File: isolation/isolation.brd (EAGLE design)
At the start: 74.5 x 72.7 mm, 91 parts, among them IC1 XTLV61048DBVR, IC2 SN74HC14PWR, IC3 SN74HCS32BQAR, IC4 SN74HCS08DYYR, IC5 FDN359BN, IC6 FDN359BN, IC7 FDN359BN, IC8 FDN359BN, J1 S4B-PH-K-S(LF)(SN), J2 S4B-PH-K-S(LF)(SN), J3 S2B-PH-K-S(LF)(SN), J4 S2B-PH-K-S(LF)(SN), J5 S2B-PH-K-S(LF)(SN), J7 217175-0001

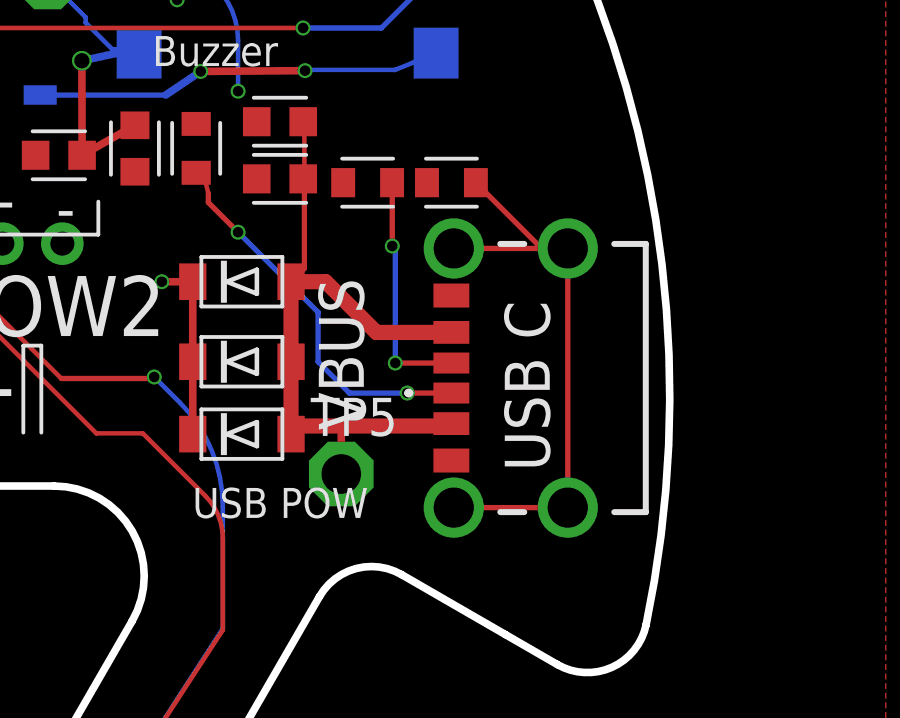
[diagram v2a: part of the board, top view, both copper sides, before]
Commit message: swap usb c (again)
now using USB4105-GF-A-120, consistent with WALLY
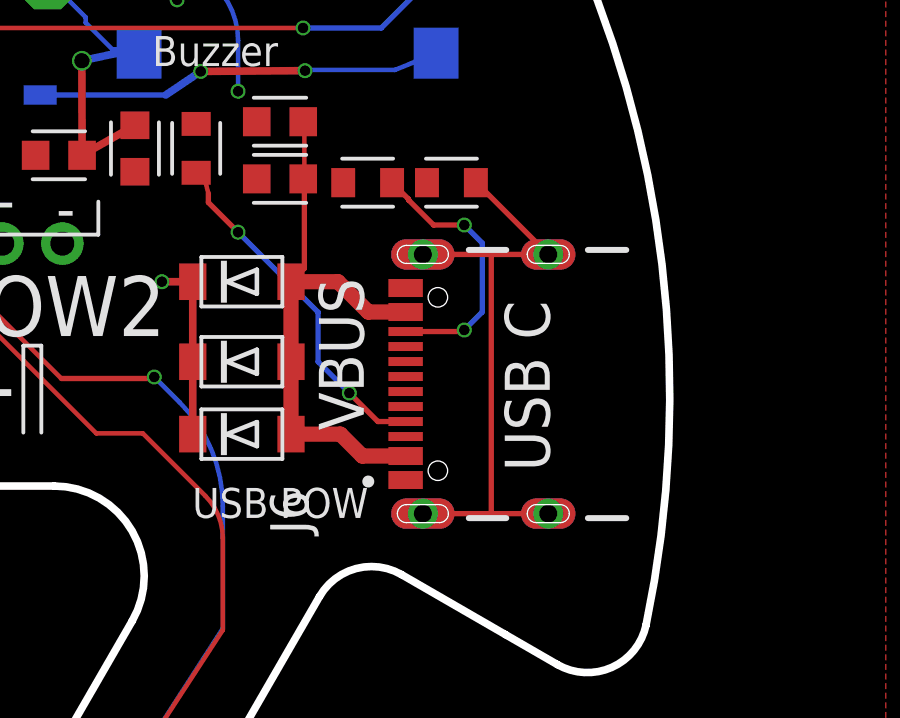
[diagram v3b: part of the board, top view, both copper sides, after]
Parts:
- removed J7: 217175-0001, SamacSys_Parts:2171750001
- removed TP5: PTR1PAD1-13, testpad:P1-13
- added J6: USB4105-GF-A, USB4105-GF-A:GCT_USB4105-GF-A
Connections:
- net CC1: now also J6.A5; no longer J7.A5
- net CC2: now also J6.B5; no longer J7.B5
- net GND: now also J6.A1_B12, J6.B1_A12; no longer J7.A12, J7.B12
- net SHLD: now also J6.SH1, J6.SH2, J6.SH3, J6.SH4; no longer J7.MH1, J7.MH2, J7.MH3, J7.MH4
- net VBUS: now also J6.A4_B9, J6.B4_A9; no longer J7.A9, J7.B9, TP5.TP
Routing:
- net VBUS: track 23.8 -> 19.0 mm
- net CC1: track 12.8 -> 11.7 mm
- net CC2: track 7.93 -> 8.99 mm
- net SHLD: track 19.3 -> 20.4 mm
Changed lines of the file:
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@@
 <attribute name="VOLTAGE_RATING" value="" x="11.318" y="21.685" size="1.778" layer="27" rot="R90" display="off"/>
 </element>
-<element name="J7" library="SamacSys_Parts" package="2171750001" value="217175-0001" x="33" y="0.6" smashed="yes" rot="R90">
-<attribute name="ARROW_PART_NUMBER" value="" x="33" y="0.6" size="1.778" layer="27" rot="R90" display="off"/>
-<attribute name="ARROW_PRICE-STOCK" value="" x="33" y="0.6" size="1.778" layer="27" rot="R90" display="off"/>
-<attribute name="DESCRIPTION" value="Connector USB Type C Female 6Positions 0.5mm Right Angle SMT Embossed T/R - Tape and Reel" x="33" y="0.6" size="1.778" layer="27" rot="R90" display="off"/>
-<attribute name="HEIGHT" value="3.46mm" x="33" y="0.6" size="1.778" layer="27" rot="R90" display="off"/>
-<attribute name="MANUFACTURER_NAME" value="Molex" x="33" y="0.6" size="1.778" layer="27" rot="R90" display="off"/>
-<attribute name="MANUFACTURER_PART_NUMBER" value="217175-0001" x="33" y="0.6" size="1.778" layer="27" rot="R90" display="off"/>
-<attribute name="MOUSER_PART_NUMBER" value="538-217175-0001" x="33" y="0.6" size="1.778" layer="27" rot="R90" display="off"/>
-<attribute name="MOUSER_PRICE-STOCK" value="https://www.mouser.co.uk/ProductDetail/Molex/217175-0001?qs=DRkmTr78QARWJMiqNnldSg%3D%3D" x="33" y="0.6" size="1.778" layer="27" rot="R90" display="off"/>
-<attribute name="VALUE" x="32.748" y="0.6" size="1.27" layer="27" rot="R90" align="center"/>
-</element>
-<element name="TP5" library="testpad" library_urn="urn:adsk.eagle:library:385" package="P1-13" package3d_urn="urn:adsk.eagle:package:27946/1" override_package3d_urn="urn:adsk.eagle:package:44099355/2" override_package_urn="urn:adsk.eagle:footprint:27902/1" value="PTR1PAD1-13" x="26.3" y="-2.6" smashed="yes">
-<attribute name="NAME" x="25.284" y="-1.33" size="1.27" layer="25" ratio="10"/>
-<attribute name="POPULARITY" value="2" x="26.3" y="-2.6" size="1.778" layer="27" display="off"/>
-<attribute name="TP_SIGNAL_NAME" value="" x="26.3" y="-2.6" size="1.778" layer="27" display="off"/>
-<attribute name="VALUE" x="26.3" y="-2.6" size="0.0254" layer="27"/>
+<element name="J6" library="USB4105-GF-A" package="GCT_USB4105-GF-A" value="USB4105-GF-A" x="33.2" y="0.4" smashed="yes" rot="R90">
+<attribute name="CHECK_PRICES" value="https://www.snapeda.com/parts/USB4105GFA/Global+Connector+Technology/view-part/?ref=eda" x="33.2" y="0.4" size="1.778" layer="27" rot="R90" display="off"/>
+<attribute name="DESCRIPTION" value=" USB-C (USB TYPE-C) USB 2.0 Receptacle Connector 24 (16+8 Dummy) Position Surface Mount, Right Angle; Through Hole " x="33.2" y="0.4" size="1.778" layer="27" rot="R90" display="off"/>
+<attribute name="DIGIKEY_PART_NUMBER" value="2073-USB4105-GF-ATR-ND" x="33.2" y="0.4" size="1.778" layer="27" rot="R90" display="off"/>
+<attribute name="MF" value="Global Connector Technology" x="33.2" y="0.4" size="1.778" layer="27" rot="R90" display="off"/>
+<attribute name="MP" value="USB4105GFA" x="33.2" y="0.4" size="1.778" layer="27" rot="R90" display="off"/>
+<attribute name="NAME" x="25.2" y="-4.6" size="1.27" layer="25" rot="R90"/>
+<attribute name="PACKAGE" value="None" x="33.2" y="0.4" size="1.778" layer="27" rot="R90" display="off"/>
+<attribute name="SNAPEDA_LINK" value="https://www.snapeda.com/parts/USB4105GFA/Global+Connector+Technology/view-part/?ref=snap" x="33.2" y="0.4" size="1.778" layer="27" rot="R90" display="off"/>
+<attribute name="VALUE" x="26.7" y="-4.6" size="1.27" layer="27" rot="R90"/>
 </element>
 </elements>
@@
 <contactref element="C22" pad="1"/>
 <wire x1="-7.493" y1="18.3006" x2="-8.89" y2="16.51" width="0.1778" layer="1"/>
-<contactref element="J7" pad="A12"/>
-<contactref element="J7" pad="B12"/>
+<contactref element="J6" pad="A1_B12"/>
+<contactref element="J6" pad="B1_A12"/>
 </signal>
 <signal name="VBAT">
@@
 <signal name="SHLD">
 <contactref element="R13" pad="1"/>
-<contactref element="J7" pad="MH4"/>
-<contactref element="J7" pad="MH1"/>
-<contactref element="J7" pad="MH2"/>
-<contactref element="J7" pad="MH3"/>
-<wire x1="30.05" y1="-3.72" x2="33.85" y2="-3.72" width="0.1778" layer="1"/>
-<wire x1="33.85" y1="-3.72" x2="33.85" y2="4.92" width="0.1778" layer="1"/>
-<wire x1="33.85" y1="4.92" x2="33" y2="4.92" width="0.1778" layer="1"/>
-<wire x1="32.9792" y1="4.92" x2="30.05" y2="4.92" width="0.1778" layer="1"/>
-<wire x1="30.7872" y1="7.112" x2="32.9792" y2="4.92" width="0.1778" layer="1"/>
-<wire x1="32.9792" y1="4.92" x2="33" y2="4.92" width="0.1778" layer="1"/>
+<contactref element="J6" pad="SH2"/>
+<contactref element="J6" pad="SH3"/>
+<contactref element="J6" pad="SH4"/>
+<contactref element="J6" pad="SH1"/>
+<wire x1="29.02" y1="-3.92" x2="31.3" y2="-3.92" width="0.1778" layer="1"/>
+<wire x1="31.3" y1="-3.92" x2="33.2" y2="-3.92" width="0.1778" layer="1"/>
+<wire x1="29.02" y1="4.72" x2="31.3" y2="4.72" width="0.1778" layer="1"/>
+<wire x1="31.3" y1="4.72" x2="33.2" y2="4.72" width="0.1778" layer="1"/>
+<wire x1="33.2" y1="4.72" x2="30.808" y2="7.112" width="0.1778" layer="1"/>
+<wire x1="30.808" y1="7.112" x2="30.7872" y2="7.112" width="0.1778" layer="1"/>
+<wire x1="31.3" y1="4.72" x2="31.3" y2="-3.92" width="0.1778" layer="1"/>
 </signal>
 <signal name="CC2">
 <contactref element="R12" pad="1"/>
-<contactref element="J7" pad="B5"/>
 <wire x1="27.9932" y1="7.112" x2="28" y2="7.1052" width="0.1778" layer="1"/>
-<wire x1="28" y1="7.1052" x2="28" y2="5" width="0.1778" layer="1"/>
-<via x="28" y="5" extent="1-16" drill="0.35"/>
-<wire x1="28" y1="5" x2="28.1" y2="4.9" width="0.1778" layer="16"/>
-<wire x1="28.1" y1="4.9" x2="28.1" y2="1.1" width="0.1778" layer="16"/>
-<via x="28.1" y="1.1" extent="1-16" drill="0.35"/>
-<wire x1="28.1" y1="1.1" x2="29.97" y2="1.1" width="0.1778" layer="1"/>
+<contactref element="J6" pad="B5"/>
+<via x="30.4" y="5.7" extent="1-16" drill="0.35"/>
+<wire x1="27.9932" y1="7.112" x2="28.54155" y2="6.56365" width="0.1778" layer="1"/>
+<wire x1="28.54155" y1="6.56365" x2="28.54155" y2="6.53561875" width="0.1778" layer="1"/>
+<wire x1="28.54155" y1="6.53561875" x2="29.37716875" y2="5.7" width="0.1778" layer="1"/>
+<wire x1="29.37716875" y1="5.7" x2="30.4" y2="5.7" width="0.1778" layer="1"/>
+<wire x1="30.4" y1="5.7" x2="31" y2="5.1" width="0.1778" layer="16"/>
+<wire x1="31" y1="2.8" x2="30.4" y2="2.2" width="0.1778" layer="16"/>
+<via x="30.4" y="2.2" extent="1-16" drill="0.35"/>
+<wire x1="30.4" y1="2.2" x2="30.35" y2="2.15" width="0.1778" layer="1"/>
+<wire x1="30.35" y1="2.15" x2="28.445" y2="2.15" width="0.1778" layer="1"/>
+<wire x1="31" y1="5.1" x2="31" y2="2.8" width="0.1778" layer="16"/>
 </signal>
 <signal name="CC1">
@@
 <wire x1="25.527" y1="2.794" x2="25.527" y2="1.143" width="0.1778" layer="16"/>
 <wire x1="25.527" y1="2.794" x2="22.86" y2="5.461" width="0.1778" layer="16"/>
-<contactref element="J7" pad="A5"/>
 <wire x1="25.527" y1="1.143" x2="26.57" y2="0.1" width="0.1778" layer="16"/>
-<wire x1="26.57" y1="0.1" x2="28.5" y2="0.1" width="0.1778" layer="16"/>
-<via x="28.5" y="0.1" extent="1-16" drill="0.35"/>
-<wire x1="28.5" y1="0.1" x2="29.97" y2="0.1" width="0.1778" layer="1"/>
+<contactref element="J6" pad="A5"/>
+<via x="26.57" y="0.1" extent="1-16" drill="0.35"/>
+<wire x1="26.57" y1="0.1" x2="27.52" y2="-0.85" width="0.1778" layer="1"/>
+<wire x1="27.52" y1="-0.85" x2="28.445" y2="-0.85" width="0.1778" layer="1"/>
 </signal>
 <signal name="VBUS">
@@
 <wire x1="25.0698" y1="4.2553" x2="25.0698" y2="7.112" width="0.1778" layer="1"/>
 <wire x1="25.0698" y1="4.2553" x2="24.6245" y2="3.81" width="0.1778" layer="1"/>
-<wire x1="24.6245" y1="3.81" x2="25.781" y2="3.81" width="0.508" layer="1"/>
 <wire x1="24.6245" y1="1.143" x2="24.6245" y2="3.81" width="0.508" layer="1"/>
-<contactref element="J7" pad="A9"/>
-<contactref element="J7" pad="B9"/>
-<wire x1="27.471" y1="2.12" x2="29.97" y2="2.12" width="0.508" layer="1"/>
-<wire x1="25.781" y1="3.81" x2="27.471" y2="2.12" width="0.508" layer="1"/>
-<wire x1="29.97" y1="-0.92" x2="29.89" y2="-1" width="0.508" layer="1"/>
-<contactref element="TP5" pad="TP"/>
 <wire x1="24.6245" y1="1.143" x2="24.6245" y2="-1.27" width="0.508" layer="1"/>
-<wire x1="24.8945" y1="-1" x2="24.6245" y2="-1.27" width="0.508" layer="1"/>
-<wire x1="29.89" y1="-1" x2="26.3" y2="-1" width="0.508" layer="1"/>
-<wire x1="26.3" y1="-1" x2="24.8945" y2="-1" width="0.508" layer="1"/>
-<wire x1="26.3" y1="-2.6" x2="26.3" y2="-1" width="0.254" layer="1"/>
+<contactref element="J6" pad="A4_B9"/>
+<contactref element="J6" pad="B4_A9"/>
+<wire x1="27" y1="-2" x2="28.445" y2="-2" width="0.508" layer="1"/>
+<wire x1="24.6245" y1="-1.27" x2="26.27" y2="-1.27" width="0.508" layer="1"/>
+<wire x1="26.27" y1="-1.27" x2="27" y2="-2" width="0.508" layer="1"/>
+<wire x1="28.445" y1="2.8" x2="27.2" y2="2.8" width="0.508" layer="1"/>
+<wire x1="26.19" y1="3.81" x2="24.6245" y2="3.81" width="0.508" layer="1"/>
+<wire x1="27.2" y1="2.8" x2="26.19" y2="3.81" width="0.508" layer="1"/>
 </signal>
 <signal name="N$27">
@@
 <mfgpreviewcolor name="substratecolor" color="0xFF786E46"/>
 </mfgpreviewcolors>
+<errors>
+</errors>
 </board>
 </drawing>

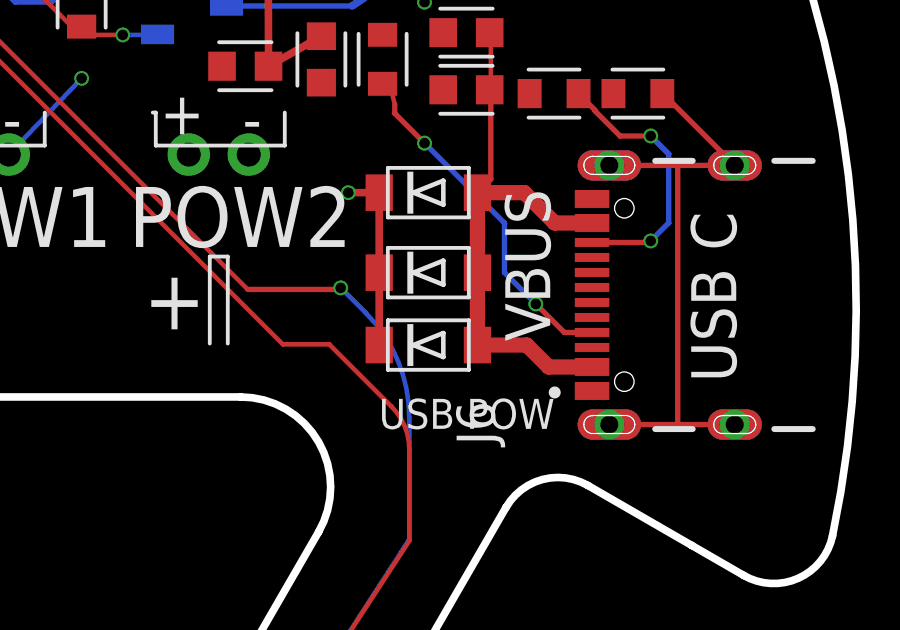
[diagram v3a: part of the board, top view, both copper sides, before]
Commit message: remove parallel vbus diodes
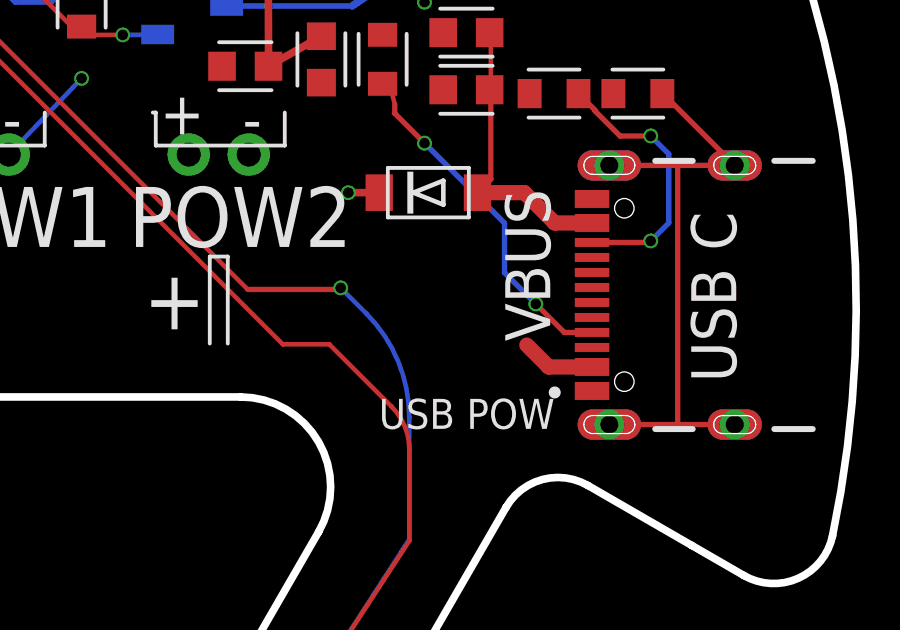
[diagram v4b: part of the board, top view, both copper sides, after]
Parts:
- removed D3, D4: USBDiode, adafruit:SOD-123FL
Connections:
- net VBAT: no longer D3.C, D4.C
- net VBUS: no longer D3.A, D4.A
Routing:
- net VBUS: track 19.0 -> 12.3 mm
- net VBAT: track 60.9 -> 55.8 mm
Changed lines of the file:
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@@
 <layer number="44" name="Drills" color="7" fill="1" visible="no" active="yes"/>
 <layer number="45" name="Holes" color="7" fill="1" visible="yes" active="yes"/>
-<layer number="46" name="Milling" color="3" fill="1" visible="no" active="yes"/>
+<layer number="46" name="Milling" color="3" fill="1" visible="yes" active="yes"/>
 <layer number="47" name="Measures" color="7" fill="1" visible="no" active="yes"/>
 <layer number="48" name="Document" color="7" fill="1" visible="no" active="yes"/>
@@
 <attribute name="VALUE" x="20.447" y="1.524" size="0.4064" layer="27" font="vector"/>
 </element>
-<element name="D3" library="adafruit" library_urn="urn:adsk.eagle:library:420" package="SOD-123FL" package3d_urn="urn:adsk.eagle:package:6240937/1" override_package3d_urn="urn:adsk.eagle:package:44099334/2" override_package_urn="urn:adsk.eagle:footprint:6240294/1" value="USBDiode" x="22.987" y="1.143" smashed="yes">
-<attribute name="VALUE" x="21.887" y="-0.141" size="0.4064" layer="27"/>
-</element>
-<element name="D4" library="adafruit" library_urn="urn:adsk.eagle:library:420" package="SOD-123FL" package3d_urn="urn:adsk.eagle:package:6240937/1" override_package3d_urn="urn:adsk.eagle:package:44099339/2" override_package_urn="urn:adsk.eagle:footprint:6240294/1" value="USBDiode" x="22.987" y="-1.27" smashed="yes">
-<attribute name="VALUE" x="21.887" y="-2.554" size="0.4064" layer="27"/>
-</element>
 <element name="C14" library="Capacitor" library_urn="urn:adsk.eagle:library:16290819" package="CAPC1608X85" package3d_urn="urn:adsk.eagle:package:16290898/5" value="100n" x="24.257" y="7.239" smashed="yes">
 <attribute name="CATEGORY" value="Capacitor" x="25.527" y="7.239" size="1.778" layer="27" display="off"/>
@@
 <attribute name="VOLTAGE_RATING" value="" x="11.318" y="21.685" size="1.778" layer="27" rot="R90" display="off"/>
 </element>
-<element name="J6" library="USB4105-GF-A" package="GCT_USB4105-GF-A" value="USB4105-GF-A" x="33.2" y="0.4" smashed="yes" rot="R90">
+<element name="J6" library="USB4105-GF-A" package="GCT_USB4105-GF-A" override_package3d_urn="urn:adsk.eagle:package:44135151/2" override_package_urn="urn:adsk.eagle:footprint:44135152/1" value="USB4105-GF-A" x="33.2" y="0.4" smashed="yes" rot="R90">
 <attribute name="CHECK_PRICES" value="https://www.snapeda.com/parts/USB4105GFA/Global+Connector+Technology/view-part/?ref=eda" x="33.2" y="0.4" size="1.778" layer="27" rot="R90" display="off"/>
 <attribute name="DESCRIPTION" value=" USB-C (USB TYPE-C) USB 2.0 Receptacle Connector 24 (16+8 Dummy) Position Surface Mount, Right Angle; Through Hole " x="33.2" y="0.4" size="1.778" layer="27" rot="R90" display="off"/>
@@
 <attribute name="MF" value="Global Connector Technology" x="33.2" y="0.4" size="1.778" layer="27" rot="R90" display="off"/>
 <attribute name="MP" value="USB4105GFA" x="33.2" y="0.4" size="1.778" layer="27" rot="R90" display="off"/>
-<attribute name="NAME" x="25.2" y="-4.6" size="1.27" layer="25" rot="R90"/>
 <attribute name="PACKAGE" value="None" x="33.2" y="0.4" size="1.778" layer="27" rot="R90" display="off"/>
 <attribute name="SNAPEDA_LINK" value="https://www.snapeda.com/parts/USB4105GFA/Global+Connector+Technology/view-part/?ref=snap" x="33.2" y="0.4" size="1.778" layer="27" rot="R90" display="off"/>
@@
 <contactref element="IC4" pad="14"/>
 <contactref element="D2" pad="C"/>
-<contactref element="D4" pad="C"/>
-<contactref element="D3" pad="C"/>
 <contactref element="BAT1" pad="1"/>
 <contactref element="TP2" pad="TP"/>
@@
 <wire x1="-12.798875" y1="24.031125" x2="-12.56016875" y2="24.13" width="0.1524" layer="1" curve="-45"/>
 <wire x1="-12.56016875" y1="24.13" x2="-11.43" y2="24.13" width="0.1524" layer="1"/>
-<wire x1="21.3495" y1="-1.27" x2="21.3495" y2="1.143" width="0.254" layer="1"/>
-<wire x1="21.3495" y1="1.143" x2="21.3495" y2="3.81" width="0.254" layer="1"/>
 <wire x1="21.3495" y1="3.81" x2="20.32" y2="3.81" width="0.254" layer="1"/>
 <via x="20.32" y="3.81" extent="1-16" drill="0.35"/>
@@
 <wire x1="-10.795" y1="15.748" x2="-10.734259375" y2="15.687259375" width="0.1778" layer="1"/>
 <wire x1="-8.6868" y1="15.4686" x2="-10.734259375" y2="15.687259375" width="0.1778" layer="1"/>
+<wire x1="8.663871875" y1="23.442871875" x2="20.8026" y2="20.3962" width="0" layer="19" extent="1-1"/>
+<wire x1="4.318" y1="22.0854" x2="5.842" y2="22.225" width="0" layer="19" extent="1-1"/>
+<wire x1="-10.922" y1="24.8694" x2="-8.001" y2="22.0854" width="0" layer="19" extent="1-1"/>
+<wire x1="-16.51" y1="22.9744" x2="-13.204" y2="22.863" width="0" layer="19" extent="1-16"/>
+<wire x1="-8.6868" y1="15.4686" x2="-4.572" y2="19.519" width="0" layer="19" extent="1-1"/>
+<wire x1="-11.454" y1="16.778" x2="-10.795" y2="15.748" width="0" layer="19" extent="16-16"/>
+<wire x1="-16.51" y1="14.3636" x2="-11.454" y2="16.778" width="0" layer="19" extent="1-16"/>
+<wire x1="-20.297325" y1="13.865675" x2="-17.6022" y2="13.6906" width="0" layer="19" extent="1-1"/>
+<wire x1="-28.448" y1="19.05" x2="-22.27" y2="15.985" width="0" layer="19" extent="16-16"/>
+<wire x1="7.001" y1="5.08" x2="4.318" y2="20.4596" width="0" layer="19" extent="1-1"/>
+<wire x1="15.002" y1="5.08" x2="7.001" y2="5.08" width="0" layer="19" extent="1-1"/>
+<wire x1="20.32" y1="3.81" x2="15.002" y2="5.08" width="0" layer="19" extent="1-1"/>
+<wire x1="-26.924" y1="-0.635" x2="-22.10248125" y2="14.5006" width="0" layer="19" extent="1-1"/>
+<wire x1="14.224" y1="-30.988" x2="20.32" y2="3.81" width="0" layer="19" extent="1-1"/>
 </signal>
 <signal name="N$1">
@@
 <signal name="VBUS">
 <contactref element="D2" pad="A"/>
-<contactref element="D3" pad="A"/>
-<contactref element="D4" pad="A"/>
 <contactref element="C14" pad="2"/>
 <contactref element="C15" pad="2"/>
@@
 <wire x1="25.0698" y1="4.2553" x2="25.0698" y2="7.112" width="0.1778" layer="1"/>
 <wire x1="25.0698" y1="4.2553" x2="24.6245" y2="3.81" width="0.1778" layer="1"/>
-<wire x1="24.6245" y1="1.143" x2="24.6245" y2="3.81" width="0.508" layer="1"/>
-<wire x1="24.6245" y1="1.143" x2="24.6245" y2="-1.27" width="0.508" layer="1"/>
 <contactref element="J6" pad="A4_B9"/>
 <contactref element="J6" pad="B4_A9"/>
 <wire x1="27" y1="-2" x2="28.445" y2="-2" width="0.508" layer="1"/>
-<wire x1="24.6245" y1="-1.27" x2="26.27" y2="-1.27" width="0.508" layer="1"/>
 <wire x1="26.27" y1="-1.27" x2="27" y2="-2" width="0.508" layer="1"/>
 <wire x1="28.445" y1="2.8" x2="27.2" y2="2.8" width="0.508" layer="1"/>
 <wire x1="26.19" y1="3.81" x2="24.6245" y2="3.81" width="0.508" layer="1"/>
 <wire x1="27.2" y1="2.8" x2="26.19" y2="3.81" width="0.508" layer="1"/>
+<wire x1="28.445" y1="2.8" x2="26.27" y2="-1.27" width="0" layer="19" extent="1-1"/>
 </signal>
 <signal name="N$27">
